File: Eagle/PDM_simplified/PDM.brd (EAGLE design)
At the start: 101.3 x 76.2 mm, 29 parts

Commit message: Python Image Comparison
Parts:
- moved BATT1_W 9.55 mm to (42.5, 19.7)
- moved D2 5.12 mm to (50.8, 23.5)
- moved R8 5.12 mm to (55.9, 23.5)
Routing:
- net N$18: track 13.7 -> 21.2 mm
- net GND: track 35.9 -> 39.6 mm
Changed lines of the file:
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@@
 </element>
 <element name="R7" library="rcl" package="R1206" value="15.4K" x="60.96" y="34.29" rot="R90"/>
-<element name="R8" library="rcl" package="R1206" value="10K" x="60.96" y="24.13" rot="R90"/>
+<element name="R8" library="rcl" package="R1206" value="10K" x="55.88" y="23.495" rot="R90"/>
 <element name="C5" library="rcl" package="C1206K" value="10uF" x="52.07" y="41.91" smashed="yes" rot="R90">
 <attribute name="NAME" x="50.97" y="40.945" size="1.016" layer="25" rot="R90"/>
@@
 <attribute name="VALUE" x="15.875" y="3.81" size="1.27" layer="27"/>
 </element>
-<element name="D2" library="diode" package="SMB" value="3.3V" x="55.88" y="24.13" smashed="yes" rot="R270">
-<attribute name="NAME" x="50.419" y="26.289" size="1.27" layer="25" rot="R270"/>
-<attribute name="VALUE" x="52.451" y="26.289" size="1.27" layer="27" rot="R270"/>
+<element name="D2" library="diode" package="SMB" value="3.3V" x="50.8" y="23.495" smashed="yes" rot="R270">
+<attribute name="NAME" x="45.339" y="25.654" size="1.27" layer="25" rot="R270"/>
+<attribute name="VALUE" x="47.371" y="25.654" size="1.27" layer="27" rot="R270"/>
 </element>
 <element name="DUE" library="con-molex" package="5566-2" value="" x="41.91" y="64.77">
@@
 <attribute name="VALUE" x="25.908" y="56.769" size="1.27" layer="27" ratio="10" rot="R180"/>
 </element>
-<element name="BATT1_W" library="MRSDTeamB" package="CON_XT60_PIGTAIL" value="" x="52.07" y="19.05" rot="R180"/>
+<element name="BATT1_W" library="MRSDTeamB" package="CON_XT60_PIGTAIL" value="" x="42.545" y="19.685" rot="R180"/>
 <element name="U1" library="MRSDTeamB" package="TO220V" value="" x="54.61" y="43.18" rot="R90"/>
 <element name="BATT1" library="MRSDTeamB" package="CON_XT60_PCB_MOUNT" value="" x="31.75" y="11.43" rot="R90"/>
@@
 <wire x1="57.15" y1="43.18" x2="60.96" y2="43.18" width="0.6096" layer="1"/>
 <wire x1="60.96" y1="43.18" x2="60.96" y2="42.95" width="0.6096" layer="1"/>
-<wire x1="60.96" y1="22.708" x2="55.88" y2="22.708" width="0.6096" layer="1"/>
-<wire x1="55.88" y1="22.708" x2="55.88" y2="21.93" width="0.6096" layer="1"/>
-<wire x1="55.88" y1="21.93" x2="55.88" y2="20.955" width="0.6096" layer="1"/>
-<wire x1="55.88" y1="20.955" x2="53.975" y2="19.05" width="0.6096" layer="1"/>
+<wire x1="55.88" y1="22.073" x2="50.8" y2="22.073" width="0.6096" layer="1"/>
+<wire x1="50.8" y1="22.073" x2="50.8" y2="21.295" width="0.6096" layer="1"/>
+<wire x1="50.8" y1="21.295" x2="50.8" y2="20.32" width="0.6096" layer="1"/>
+<wire x1="50.8" y1="20.32" x2="44.45" y2="19.685" width="0.6096" layer="1"/>
 <via x="34.29" y="53.34" extent="1-16" drill="0.6" shape="square"/>
 <wire x1="36.6" y1="53.34" x2="34.29" y2="53.34" width="0.6096" layer="1"/>
@@
 <wire x1="4.445" y1="53.34" x2="19.685" y2="53.34" width="0" layer="19" extent="1-1"/>
 <wire x1="52.07" y1="43.41" x2="36.6" y2="53.34" width="0" layer="19" extent="1-1"/>
-<wire x1="60.96" y1="22.708" x2="60.96" y2="42.95" width="0" layer="19" extent="1-1"/>
-<wire x1="81.76" y1="22.86" x2="60.96" y2="22.708" width="0" layer="19" extent="1-1"/>
+<wire x1="55.88" y1="22.073" x2="57.15" y2="43.18" width="0" layer="19" extent="1-1"/>
+<wire x1="31.75" y1="7.83" x2="44.45" y2="19.685" width="0" layer="19" extent="1-1"/>
+<wire x1="17.28" y1="7.62" x2="31.75" y2="7.83" width="0" layer="19" extent="1-1"/>
+<wire x1="81.76" y1="30.48" x2="60.96" y2="42.95" width="0" layer="19" extent="1-1"/>
 <wire x1="82.55" y1="15.24" x2="81.76" y2="19.05" width="0" layer="19" extent="1-1"/>
-<wire x1="31.75" y1="7.83" x2="53.975" y2="19.05" width="0" layer="19" extent="1-1"/>
-<wire x1="17.28" y1="7.62" x2="31.75" y2="7.83" width="0" layer="19" extent="1-1"/>
 </signal>
 <signal name="N$1">
@@
 <contactref element="R8" pad="2"/>
 <contactref element="D2" pad="C"/>
-<wire x1="60.96" y1="25.552" x2="60.96" y2="29.21" width="0.6096" layer="1"/>
+<wire x1="55.88" y1="24.917" x2="60.96" y2="29.21" width="0.6096" layer="1"/>
 <wire x1="60.96" y1="29.21" x2="60.96" y2="32.868" width="0.6096" layer="1"/>
-<wire x1="55.88" y1="26.33" x2="58.42" y2="29.21" width="0.6096" layer="1"/>
+<wire x1="50.8" y1="25.695" x2="58.42" y2="29.21" width="0.6096" layer="1"/>
 <wire x1="58.42" y1="29.21" x2="60.96" y2="29.21" width="0.6096" layer="1"/>
 </signal>
@@
 <vertex x="17.78" y="11.43"/>
 <vertex x="17.78" y="22.86"/>
-<vertex x="49.53" y="22.86"/>
-<vertex x="52.07" y="20.32"/>
-<vertex x="52.07" y="12.7"/>
-<vertex x="50.8" y="11.43"/>
-</polygon>
-<wire x1="31.75" y1="15.03" x2="50.165" y2="19.05" width="0" layer="19" extent="1-1"/>
+<vertex x="42.545" y="22.225"/>
+<vertex x="42.545" y="11.43"/>
+</polygon>
+<wire x1="31.75" y1="15.03" x2="40.64" y2="19.685" width="0" layer="19" extent="1-1"/>
 <wire x1="21.64" y1="15.26" x2="31.75" y2="15.03" width="0" layer="19" extent="1-1"/>
 <wire x1="21.64" y1="17.76" x2="21.64" y2="15.26" width="0" layer="19" extent="1-1"/>

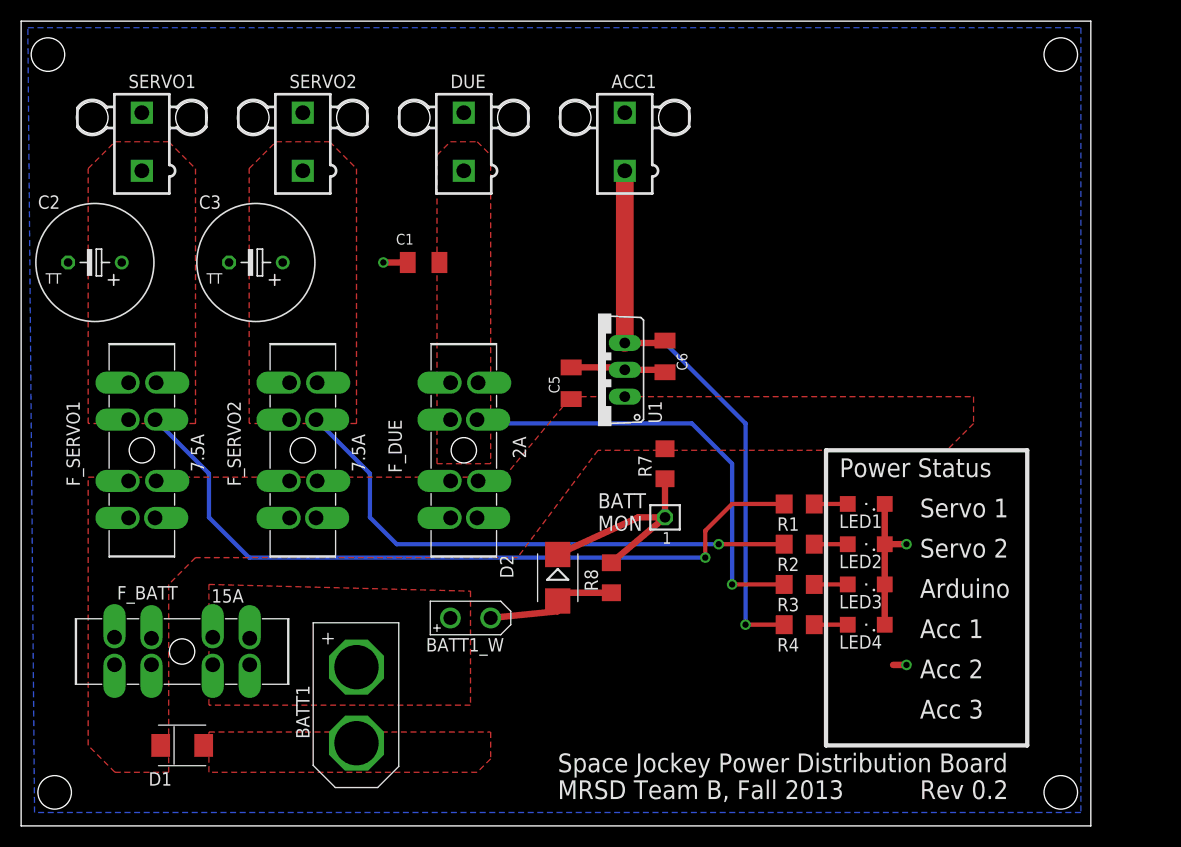
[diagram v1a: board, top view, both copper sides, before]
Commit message: Updated PDM
1 Power Supply channel
1 servo channel
1 camera channel
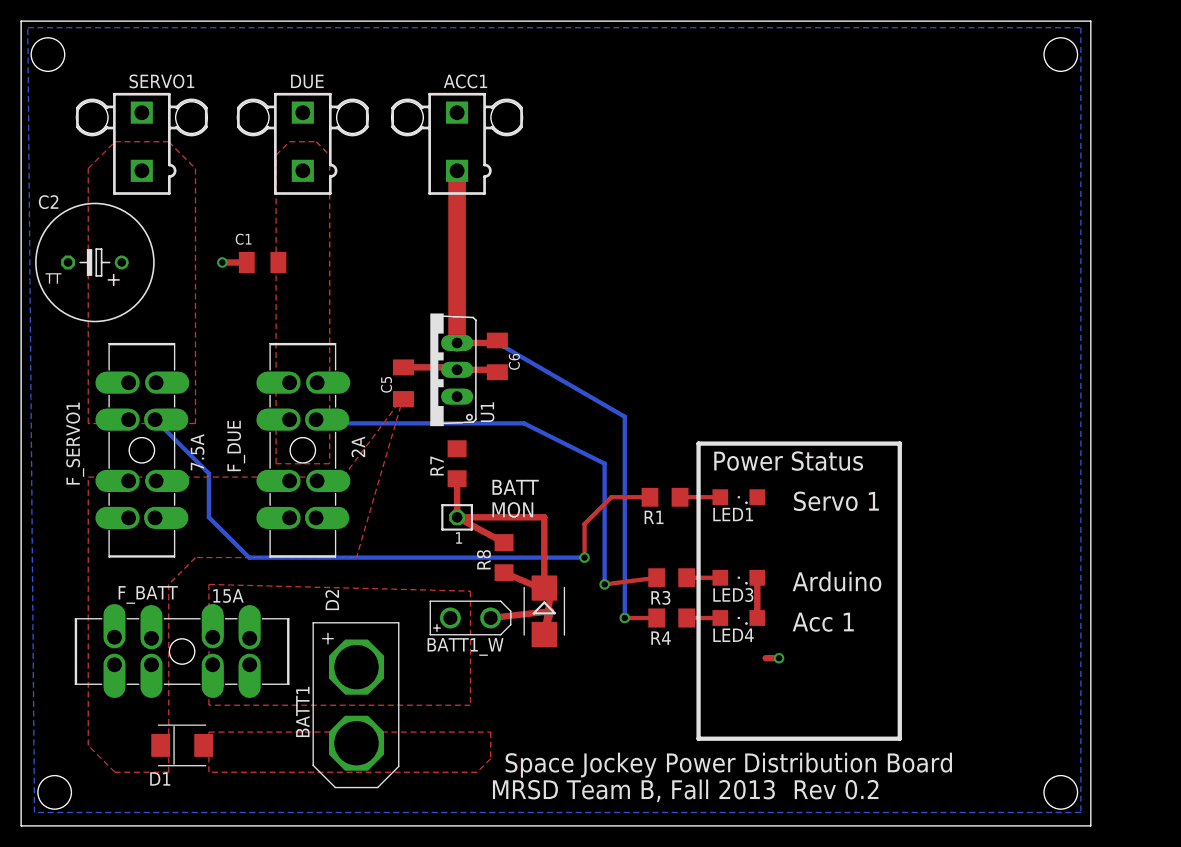
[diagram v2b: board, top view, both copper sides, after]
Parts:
- removed C3: (no value), rcl:TT5D11
- removed F_SERVO2: 7.5A, MRSDTeamB:ATO
- removed LED2: (no value), led:SML1206
- removed R2: 1K, rcl:R1206
- removed SERVO2: (no value), con-molex:5566-2
- moved BAT_MON 19.7 mm to (41.3, 29.2)
- moved R7 19.7 mm to (41.3, 34.3)
- moved ACC1 15.9 mm to (41.3, 64.8)
- moved C5 15.9 mm to (36.2, 41.9)
- moved C6 15.9 mm to (45.1, 44.5)
- moved U1 15.9 mm to (38.7, 43.2)
- moved C1 15.2 mm to (22.9, 53.3)
- moved DUE 15.2 mm to (26.7, 64.8)
- moved F_DUE 15.2 mm to (26.7, 35.6)
- moved R1 12.7 mm to (61.0, 31.1)
- moved LED1 12.1 mm to (67.9, 31.1)
- moved LED3 12.1 mm to (67.9, 23.5)
- moved LED4 12.1 mm to (67.9, 19.7)
- moved R3 12.1 mm to (61.6, 23.5)
- moved R4 12.1 mm to (61.6, 19.7)
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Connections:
- removed net N$1: C3.+, F_SERVO2.B1, F_SERVO2.B2, F_SERVO2.B3, F_SERVO2.B4, R2.2, SERVO2.1
- removed net N$8: LED2.A, R2.1
- net GND: no longer C3.-, LED2.C, SERVO2.2
- net V_SUPPLY: no longer F_SERVO2.A1, F_SERVO2.A2, F_SERVO2.A3, F_SERVO2.A4
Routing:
- net N$1: track 51.6 -> 0.00 mm, vias 1 -> 0
- net N$15: track 71.0 -> 58.9 mm
- net GND: track 39.6 -> 33.6 mm, vias 3 -> 2
- net N$8: track 3.18 -> 0.00 mm
- net N$4: track 42.2 -> 44.8 mm
- net N$6: track 57.6 -> 60.2 mm
- net N$18: track 21.2 -> 23.6 mm
- net N$5: track 3.18 -> 3.81 mm
- removed copper zone on layer 1, net N$1
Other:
- board text removed: "Acc 2"
- board text removed: "Acc 3"
- board text removed: "Servo 2"

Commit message: Miniaturized PDM
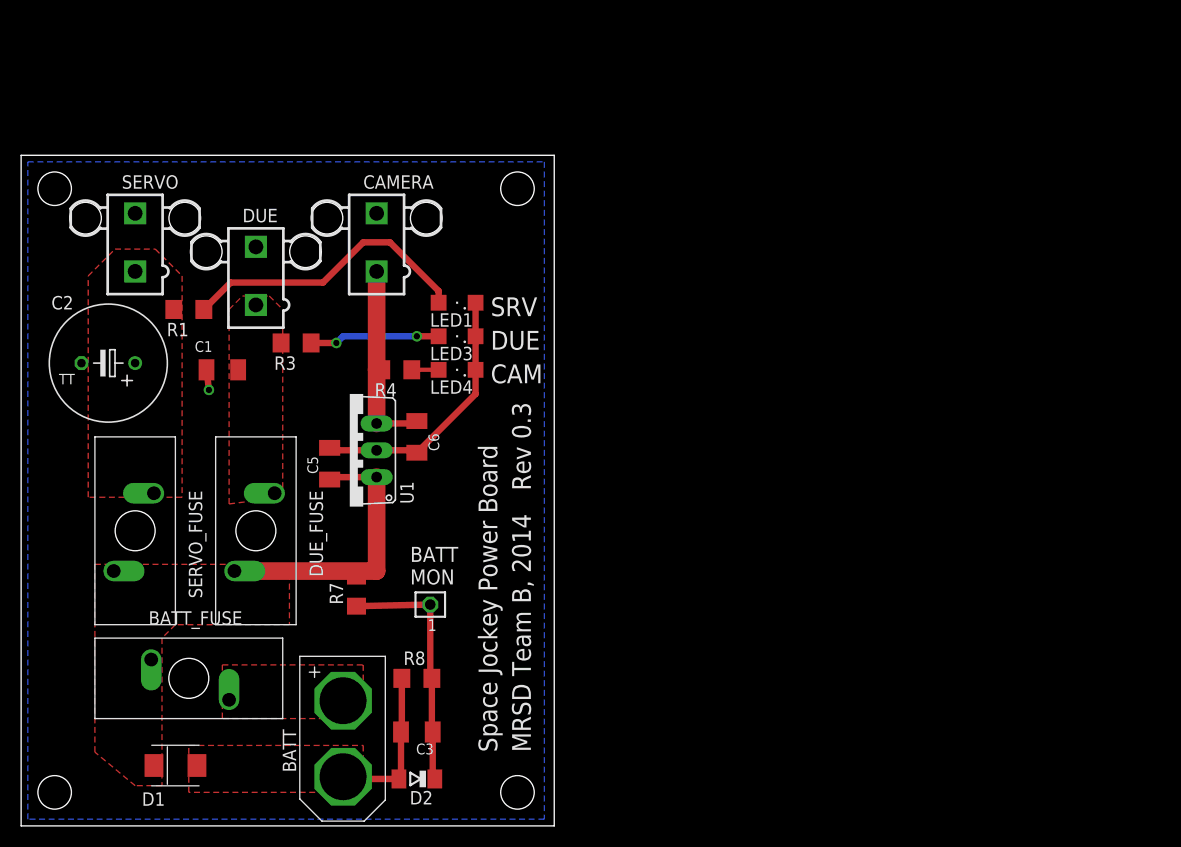
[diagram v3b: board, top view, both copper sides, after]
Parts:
- removed ACC1, SERVO1: (no value), con-molex:5566-2
- removed BATT1: (no value), MRSDTeamB:CON_XT60_PCB_MOUNT
- removed BATT1_W: (no value), MRSDTeamB:CON_XT60_PIGTAIL
- removed F_BATT: 15A, MRSDTeamB:ATO
- removed F_DUE: 2A, MRSDTeamB:ATO
- removed F_SERVO1: 7.5A, MRSDTeamB:ATO
- added BATT: (no value), MRSDTeamB:CON_XT60_PCB_MALE
- added BATT_FUSE: 10A, MRSDTeamB:MINI_ATO
- added C3: 10uF, rcl:C1206K
- added CAMERA, SERVO: (no value), con-molex:5566-2
- added DUE_FUSE: 2A, MRSDTeamB:MINI_ATO
- added SERVO_FUSE: 7.5A, MRSDTeamB:MINI_ATO
- D2: device diode:SMB -> diode:SOD80C
- R7: value 15.4K -> 1.5K
- R8: value 10K -> 1K
- moved R1 48.5 mm to (15.9, 48.9)
- moved R3 41.9 mm to (26.0, 45.7)
- moved LED4 35.5 mm to (41.3, 43.2)
- moved LED3 35.1 mm to (41.3, 46.4)
- moved R4 35.1 mm to (35.6, 43.2)
- moved LED1 32.4 mm to (41.3, 49.5)
- moved D2 19.9 mm to (37.5, 4.45), turned to 180 degrees
- moved R7 15.4 mm to (31.8, 22.2)
- moved R8 14.1 mm to (37.5, 14.0), turned to 0 degrees
- moved DUE 13.5 mm to (22.2, 52.1)
- moved C1 10.9 mm to (19.1, 43.2)
- moved C6 10.8 mm to (37.5, 36.8)
- moved U1 10.8 mm to (31.1, 35.6)
- moved C5 10.3 mm to (29.2, 34.3)
- moved C2 9.61 mm to (8.26, 43.8)
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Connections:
- net GND: now also BATT.V-, C3.2, CAMERA.2, SERVO.2; no longer ACC1.2, BATT1.V-, BATT1_W.V-, SERVO1.2
- net N$15: now also SERVO.1, SERVO_FUSE.P$3; no longer F_SERVO1.B1, F_SERVO1.B2, F_SERVO1.B3, F_SERVO1.B4, SERVO1.1
- net N$18: now also C3.1
- net N$2: now also BATT.V+, BATT_FUSE.P$2; no longer BATT1.V+, BATT1_W.V+, F_BATT.A1, F_BATT.A2, F_BATT.A3, F_BATT.A4
- net N$4: now also DUE_FUSE.P$3; no longer F_DUE.B1, F_DUE.B2, F_DUE.B3, F_DUE.B4
- net N$6: now also CAMERA.1; no longer ACC1.1
- net V_SUPPLY: now also BATT_FUSE.P$3, DUE_FUSE.P$2, SERVO_FUSE.P$2; no longer F_BATT.B1, F_BATT.B2, F_BATT.B3, F_BATT.B4, F_DUE.A1, F_DUE.A2, F_DUE.A3, F_DUE.A4, F_SERVO1.A1, F_SERVO1.A2, F_SERVO1.A3, F_SERVO1.A4
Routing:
- net N$15: track 58.9 -> 0.00 mm, vias 1 -> 0
- net N$4: track 44.8 -> 0.00 mm, vias 1 -> 0
- net N$6: track 60.2 -> 18.8 mm, vias 1 -> 0
- net V_SUPPLY: track 0.00 -> 26.8 mm
- net N$5: track 3.81 -> 27.9 mm
- net N$11: track 3.18 -> 12.3 mm, vias 0 -> 2
- net GND: track 33.6 -> 41.9 mm, vias 2 -> 1
- net N$18: track 23.6 -> 25.1 mm
- net N$13: track 3.18 -> 2.54 mm
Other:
- board size 101.3 x 76.2 mm -> 50.5 x 63.5 mm
- board text added: "CAM"
- board text added: "DUE"
- board text added: "MRSD Team B, 2014"
- board text added: "Rev 0.3"
- board text added: "SRV"
- board text added: "Space Jockey Power Board"
- board text removed: "Acc 1"
- board text removed: "Arduino"
- board text removed: "MRSD Team B, Fall 2013"
- board text removed: "Power Status"
- board text removed: "Rev 0.2"
- board text removed: "Servo 1"
- board text removed: "Space Jockey Power Distribution Board"
